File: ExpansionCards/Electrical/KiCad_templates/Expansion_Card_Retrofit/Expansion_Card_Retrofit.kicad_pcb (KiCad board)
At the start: 4 copper layers, 24 x 27.3 mm, 26 parts, among them J1 HDMI_A, P2 USB_C_Plug, U1 MS2130, U2 GD25D05CT, U3 USBLC6-2P6, Y1 Crystal

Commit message: Finished PCB design and add gerber files and BOM
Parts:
- added C4: C22uF, Capacitor_SMD:C_0201_0603Metric, B.Cu at (146.1, 139.1)
- added C5: C22uF, Capacitor_SMD:C_0201_0603Metric, B.Cu at (149.3, 139.1)
- added C6: C22uF, Capacitor_SMD:C_0201_0603Metric, B.Cu at (151.1, 132.8)
- added C7: C22uF, Capacitor_SMD:C_0201_0603Metric, B.Cu at (145.2, 130.9)
- added L1: L2.2uH, Inductor_SMD:L_0201_0603Metric, B.Cu at (146.4, 137.8)
- added L2: L2.2uH, Inductor_SMD:L_0201_0603Metric, B.Cu at (149.0, 137.8)
- added L3: L2.2uH, Inductor_SMD:L_0201_0603Metric, B.Cu at (151.1, 132.1)
- added L4: L2.2uH, Inductor_SMD:L_0201_0603Metric, B.Cu at (146.5, 131.0)
- added R10: R100K, Resistor_SMD:R_0201_0603Metric_Pad0.64x0.40mm_HandSolder, B.Cu at (147.9, 130.8)
- added R11: R680K, Resistor_SMD:R_0201_0603Metric, B.Cu at (144.1, 134.4)
- added R12: R470K, Resistor_SMD:R_0201_0603Metric, B.Cu at (150.2, 138.2)
- added R13: R100K, Resistor_SMD:R_0201_0603Metric, B.Cu at (151.1, 133.7)
- added R14: R100K, Resistor_SMD:R_0201_0603Metric, B.Cu at (151.1, 134.4)
- added R15: R150K, Resistor_SMD:R_0201_0603Metric, B.Cu at (144.1, 135.2)
- added R16: R150K, Resistor_SMD:R_0201_0603Metric, B.Cu at (151.1, 135.2)
- added R17: R150K, Resistor_SMD:R_0201_0603Metric, B.Cu at (144.2, 133.3)
- added R18: R180K, Resistor_SMD:R_0201_0603Metric, B.Cu at (144.2, 132.6)
- added U4: ~, Package_DFN_QFN:HVQFN-24-1EP_4x4mm_P0.5mm_EP2.1x2.1mm, B.Cu at (147.7, 134.4)
- moved R1 0.07 mm to (143.4, 133.5)
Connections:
- net Net-(U1-AVDD25-Pad20) renamed +2V5
- U1 pad 1: Net-(U2-VCC) -> +3.3V
- U1 pad 10: Net-(U1-AVDD11_USB-Pad10) -> +1V1
- U1 pad 12: Net-(U1-AVDD11_USB-Pad10) -> +1V1
- U1 pad 16: Net-(U2-VCC) -> +3.3V
- U1 pad 18: Net-(U1-DVDD11-Pad18) -> +1V1
- U1 pad 2: Net-(U1-AVDD33_USB-Pad2) -> +3.3V
- U1 pad 24: Net-(U1-AVDD11-Pad24) -> +1V1
- U1 pad 31: Net-(U2-VCC) -> +3.3V
- U1 pad 33: Net-(U2-VCC) -> +3.3V
- U1 pad 39: Net-(U1-DVDD11-Pad18) -> +1V1
- U1 pad 41: Net-(U2-VCC) -> +3.3V
- U1 pad 48: Net-(U1-AVDD33-Pad48) -> +3.3V
- U1 pad 5: Net-(U1-AVDD33_USB-Pad2) -> +3.3V
- U1 pad 51: Net-(U1-AVDD11-Pad24) -> +1V1
- U1 pad 52: Net-(U1-AVDD33-Pad48) -> +3.3V
- U1 pad 55: Net-(U1-AVDD11-Pad24) -> +1V1
- U1 pad 56: Net-(U1-AVDD33-Pad48) -> +3.3V
- U1 pad 59: Net-(U1-AVDD11-Pad24) -> +1V1
- U1 pad 6: Net-(U1-AVDD11_USB-Pad10) -> +1V1
- U1 pad 60: Net-(U1-AVDD33-Pad48) -> +3.3V
- U1 pad 8: Net-(U1-AVDD33_USB-Pad2) -> +3.3V
- U2 pad 3: Net-(U2-VCC) -> +3.3V
- U2 pad 8: Net-(U2-VCC) -> +3.3V
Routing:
- net +3.3V: track 0.00 -> 49.9 mm, vias 0 -> 12
- net +1V1: track 0.00 -> 47.5 mm, vias 0 -> 9
- net Net-(U2-VCC): track 31.9 -> 0.00 mm, vias 4 -> 0
- net unconnected-(J1-PadSH): track 0.00 -> 24.8 mm
- net GND: track 85.4 -> 101.2 mm, vias 9 -> 14
- net Net-(U1-AVDD11-Pad24): track 15.5 -> 0.00 mm, vias 2 -> 0
- net +2V5: track 12.4 -> 27.7 mm, vias 3 -> 4
- net +5V: track 36.2 -> 48.1 mm, vias 4 -> 9
- net Net-(U1-HDMIRXHPD): track 0.00 -> 11.5 mm, vias 1 -> 2
- net Net-(U1-DVDD11-Pad18): track 10.2 -> 0.00 mm, vias 2 -> 0
- net Net-(U1-AVDD33-Pad48): track 6.89 -> 0.00 mm, vias 4 -> 0
- net Net-(U4-EN1): track 0.00 -> 6.24 mm, vias 0 -> 2
- net Net-(U1-AVDD11_USB-Pad10): track 5.31 -> 0.00 mm, vias 3 -> 0
- net Net-(U4-FB2): track 0.00 -> 4.31 mm
- net Net-(U1-AVDD33_USB-Pad2): track 4.30 -> 0.00 mm, vias 3 -> 0
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
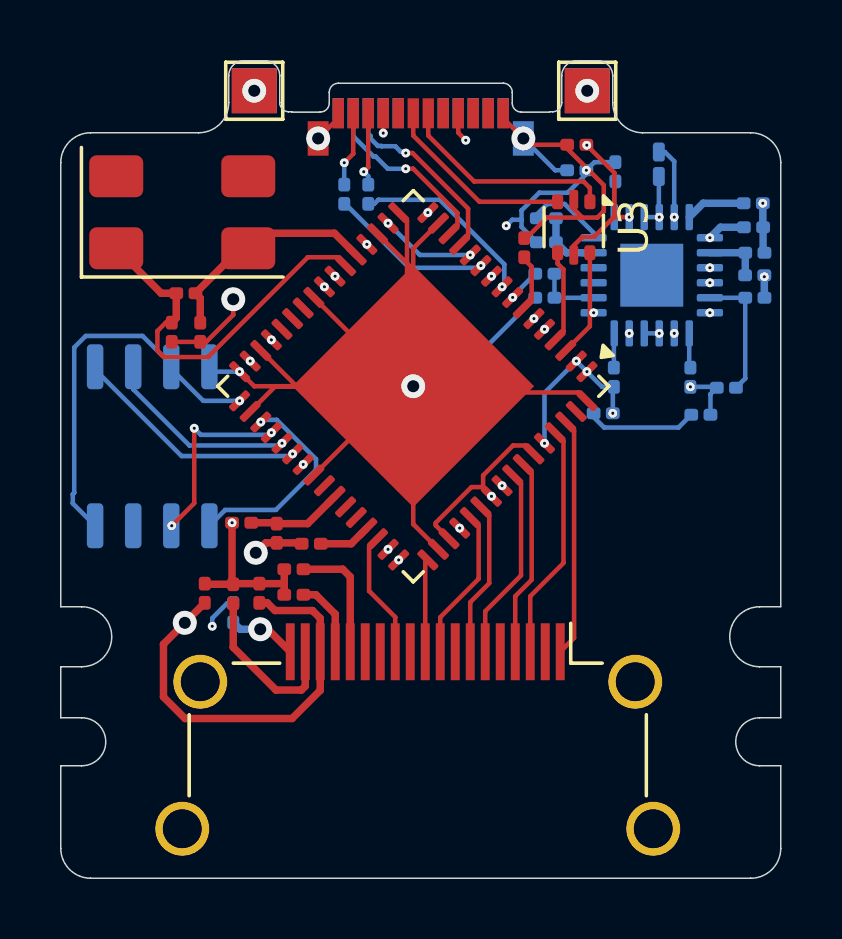
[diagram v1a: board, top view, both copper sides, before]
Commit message: Modified the USB traces to get more closely matching trace lengths
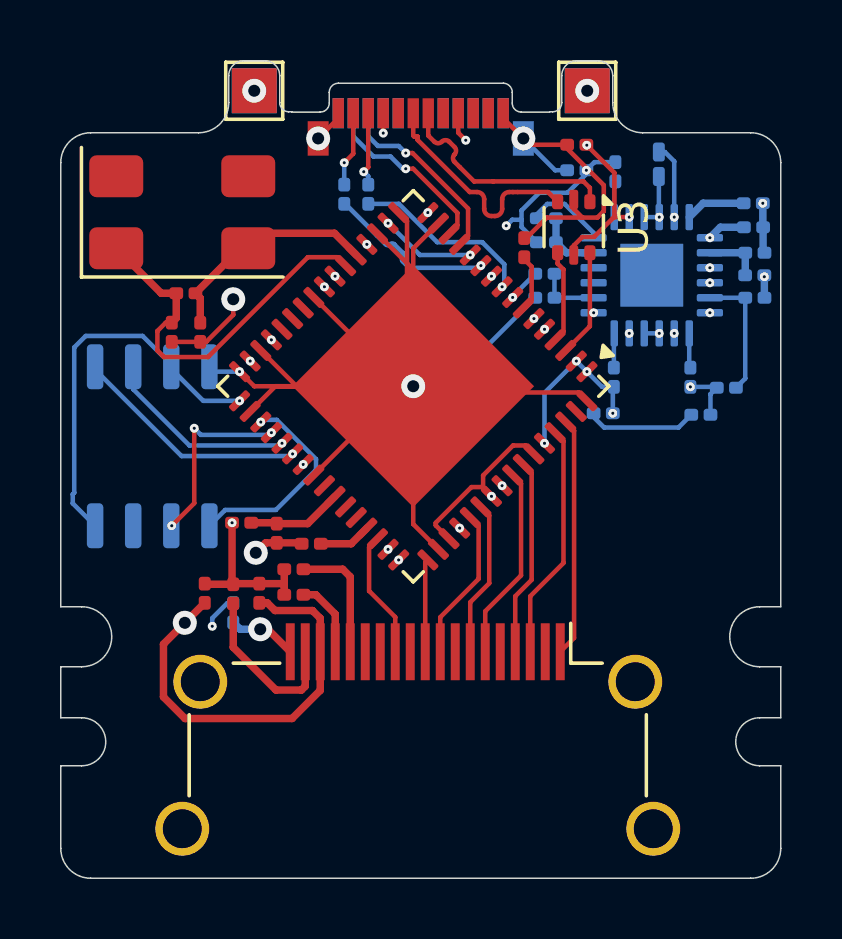
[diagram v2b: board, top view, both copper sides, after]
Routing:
- net Net-(P2-D+): track 6.47 -> 7.69 mm
